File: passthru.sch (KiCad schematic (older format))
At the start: 0 parts

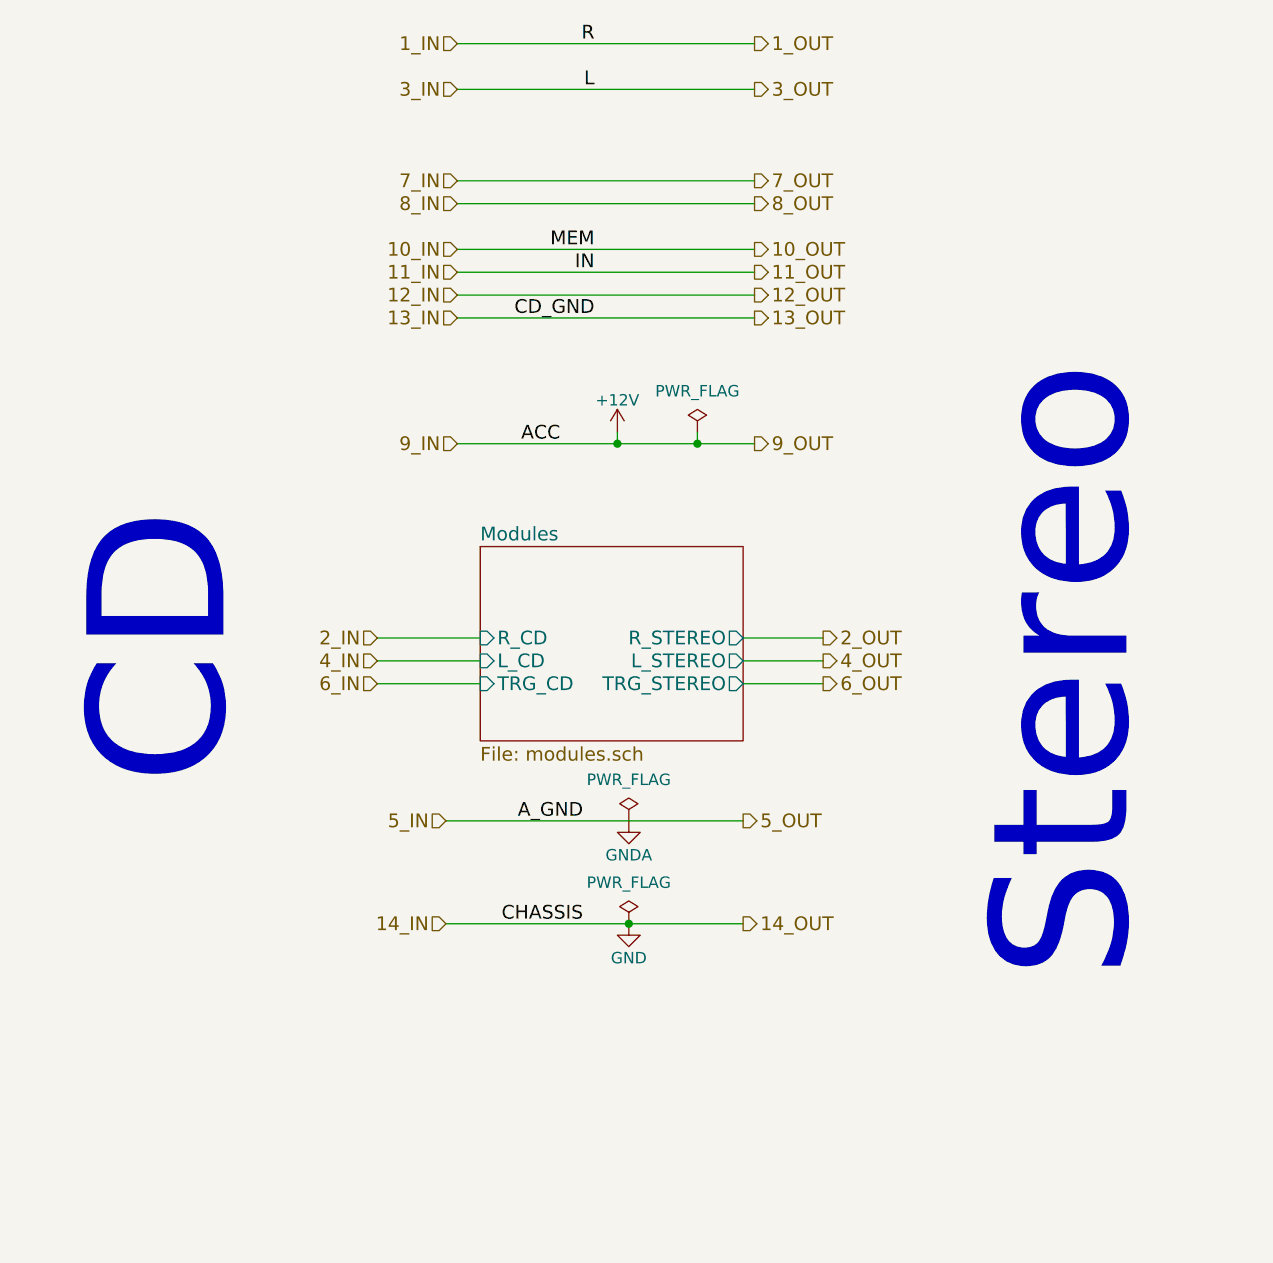
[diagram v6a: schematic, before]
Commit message: Major update to use Atmel ATTINY4313
Replace Pro Micro as microcontroller. Mostly contianed within the
control sheet.
Moved LEDs all onto control sheet.
Updated a few capacitors.
Added a reset switch. Still need to decide part.
Updated a few capacitor models for 4.0.7
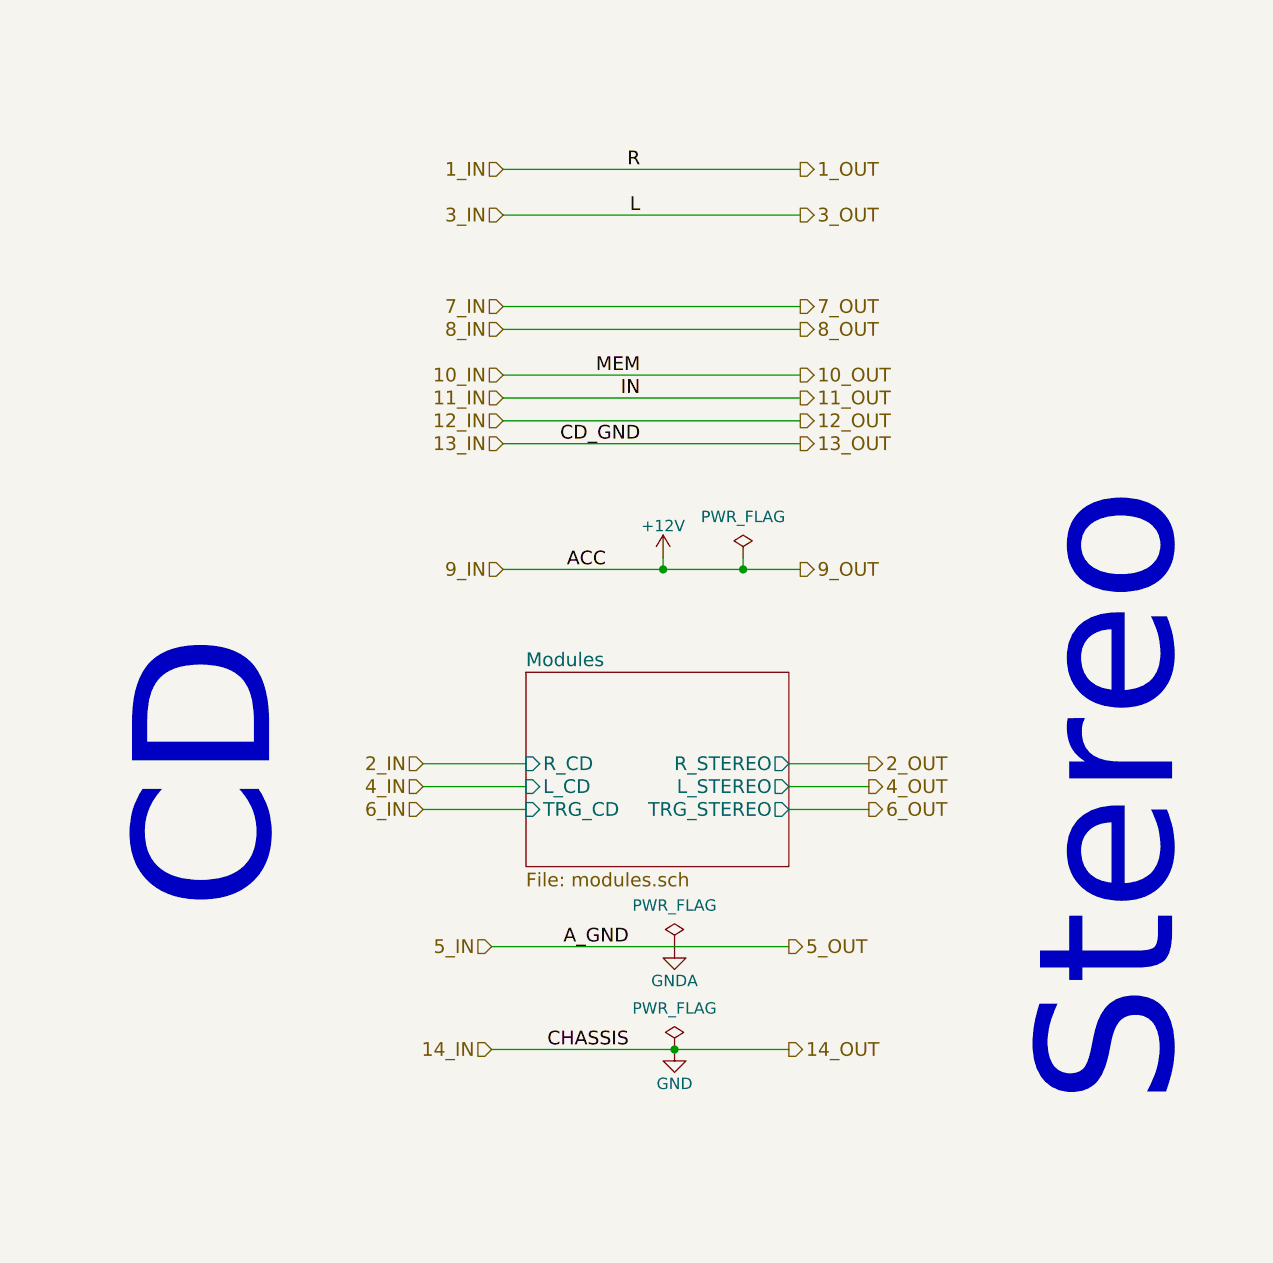
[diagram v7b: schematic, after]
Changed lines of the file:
@@
 $EndDescr
 Wire Wire Line
-	4700 1200 6000 1200
+	4900 1750 6200 1750
 Wire Wire Line
-	4700 1400 6000 1400
+	4900 1950 6200 1950
 Wire Wire Line
-	4650 4600 5950 4600
+	4850 5150 6150 5150
 Wire Wire Line
-	4700 1800 6000 1800
+	4900 2350 6200 2350
 Wire Wire Line
-	4700 1900 6000 1900
+	4900 2450 6200 2450
 Wire Wire Line
-	4700 2950 6000 2950
+	4900 3500 6200 3500
 Wire Wire Line
-	4700 2100 6000 2100
+	4900 2650 6200 2650
 Wire Wire Line
-	4700 2200 6000 2200
+	4900 2750 6200 2750
 Wire Wire Line
-	4700 2300 6000 2300
+	4900 2850 6200 2850
 Wire Wire Line
-	4700 2400 6000 2400
+	4900 2950 6200 2950
 Wire Wire Line
-	4650 5050 5950 5050
-Text HLabel 4700 1200 0    60   Input ~ 0
+	4850 5600 6150 5600
+Text HLabel 4900 1750 0    60   Input ~ 0
 1_IN
-Text HLabel 4350 3800 0    60   Input ~ 0
+Text HLabel 4550 4350 0    60   Input ~ 0
 2_IN
-Text HLabel 4700 1400 0    60   Input ~ 0
+Text HLabel 4900 1950 0    60   Input ~ 0
 3_IN
-Text HLabel 4350 3900 0    60   Input ~ 0
+Text HLabel 4550 4450 0    60   Input ~ 0
 4_IN
-Text HLabel 4650 4600 0    60   Input ~ 0
+Text HLabel 4850 5150 0    60   Input ~ 0
 5_IN
-Text HLabel 4350 4000 0    60   Input ~ 0
+Text HLabel 4550 4550 0    60   Input ~ 0
 6_IN
-Text HLabel 4700 1800 0    60   Input ~ 0
+Text HLabel 4900 2350 0    60   Input ~ 0
 7_IN
-Text HLabel 4700 1900 0    60   Input ~ 0
+Text HLabel 4900 2450 0    60   Input ~ 0
 8_IN
-Text HLabel 4700 2950 0    60   Input ~ 0
+Text HLabel 4900 3500 0    60   Input ~ 0
 9_IN
-Text HLabel 4700 2100 0    60   Input ~ 0
+Text HLabel 4900 2650 0    60   Input ~ 0
 10_IN
-Text HLabel 4700 2200 0    60   Input ~ 0
+Text HLabel 4900 2750 0    60   Input ~ 0
 11_IN
-Text HLabel 4700 2300 0    60   Input ~ 0
+Text HLabel 4900 2850 0    60   Input ~ 0
 12_IN
-Text HLabel 4700 2400 0    60   Input ~ 0
+Text HLabel 4900 2950 0    60   Input ~ 0
 13_IN
-Text HLabel 4650 5050 0    60   Input ~ 0
+Text HLabel 4850 5600 0    60   Input ~ 0
 14_IN
-Text HLabel 6000 1200 2    60   Output ~ 0
+Text HLabel 6200 1750 2    60   Output ~ 0
 1_OUT
-Text HLabel 6300 3800 2    60   Output ~ 0
+Text HLabel 6500 4350 2    60   Output ~ 0
 2_OUT
-Text HLabel 6000 1400 2    60   Output ~ 0
+Text HLabel 6200 1950 2    60   Output ~ 0
 3_OUT
-Text HLabel 6300 3900 2    60   Output ~ 0
+Text HLabel 6500 4450 2    60   Output ~ 0
 4_OUT
-Text HLabel 5950 4600 2    60   Output ~ 0
+Text HLabel 6150 5150 2    60   Output ~ 0
 5_OUT
-Text HLabel 6300 4000 2    60   Output ~ 0
+Text HLabel 6500 4550 2    60   Output ~ 0
 6_OUT
-Text HLabel 6000 1800 2    60   Output ~ 0
+Text HLabel 6200 2350 2    60   Output ~ 0
 7_OUT
-Text HLabel 6000 1900 2    60   Output ~ 0
+Text HLabel 6200 2450 2    60   Output ~ 0
 8_OUT
-Text HLabel 6000 2950 2    60   Output ~ 0
+Text HLabel 6200 3500 2    60   Output ~ 0
 9_OUT
-Text HLabel 6000 2100 2    60   Output ~ 0
+Text HLabel 6200 2650 2    60   Output ~ 0
 10_OUT
-Text HLabel 6000 2200 2    60   Output ~ 0
+Text HLabel 6200 2750 2    60   Output ~ 0
 11_OUT
-Text HLabel 6000 2300 2    60   Output ~ 0
+Text HLabel 6200 2850 2    60   Output ~ 0
 12_OUT
-Text HLabel 6000 2400 2    60   Output ~ 0
+Text HLabel 6200 2950 2    60   Output ~ 0
 13_OUT
-Text HLabel 5950 5050 2    60   Output ~ 0
+Text HLabel 6150 5600 2    60   Output ~ 0
 14_OUT
-Text Label 5300 1200 2    60   ~ 0
+Text Label 5500 1750 2    60   ~ 0
 R
-Text Label 5300 1400 2    60   ~ 0
+Text Label 5500 1950 2    60   ~ 0
 L
-Text Label 5250 4600 2    60   ~ 0
+Text Label 5450 5150 2    60   ~ 0
 A_GND
-Text Label 5150 2950 2    60   ~ 0
+Text Label 5350 3500 2    60   ~ 0
 ACC
-Text Label 5300 2100 2    60   ~ 0
+Text Label 5500 2650 2    60   ~ 0
 MEM
-Text Label 5300 2200 2    60   ~ 0
+Text Label 5500 2750 2    60   ~ 0
 IN
-Text Label 5300 2400 2    60   ~ 0
+Text Label 5500 2950 2    60   ~ 0
 CD_GND
-Text Label 5250 5050 2    60   ~ 0
+Text Label 5450 5600 2    60   ~ 0
 CHASSIS
 Wire Wire Line
-	4350 3800 4800 3800
+	4550 4350 5000 4350
 Wire Wire Line
-	4350 3900 4800 3900
+	4550 4450 5000 4450
 Wire Wire Line
-	4350 4000 4800 4000
+	4550 4550 5000 4550
 Wire Wire Line
-	5950 3800 6300 3800
+	6150 4350 6500 4350
 Wire Wire Line
-	5950 3900 6300 3900
+	6150 4450 6500 4450
 Wire Wire Line
-	5950 4000 6300 4000
+	6150 4550 6500 4550
 $Sheet
-S 4800 3400 1150 850
+S 5000 3950 1150 850
 U 58B1273D
 F0 "Modules" 60
 F1 "modules.sch" 60
-F2 "L_CD" I L 4800 3900 60
-F3 "R_CD" I L 4800 3800 60
-F4 "L_STEREO" O R 5950 3900 60
-F5 "R_STEREO" O R 5950 3800 60
-F6 "TRG_STEREO" O R 5950 4000 60
-F7 "TRG_CD" I L 4800 4000 60
+F2 "L_CD" I L 5000 4450 60
+F3 "R_CD" I L 5000 4350 60
+F4 "L_STEREO" O R 6150 4450 60
+F5 "R_STEREO" O R 6150 4350 60
+F6 "TRG_STEREO" O R 6150 4550 60
+F7 "TRG_CD" I L 5000 4550 60
 $EndSheet
 $Comp
 L GND #PWR01
 U 1 1 58B1285E
-P 5450 5050
-F 0 "#PWR01" H 5450 4800 50  0001 C CNN
-F 1 "GND" H 5450 4900 50  0000 C CNN
-F 2 "" H 5450 5050 50  0000 C CNN
-F 3 "" H 5450 5050 50  0000 C CNN
-	1    5450 5050
+P 5650 5600
+F 0 "#PWR01" H 5650 5350 50  0001 C CNN
+F 1 "GND" H 5650 5450 50  0000 C CNN
+F 2 "" H 5650 5600 50  0000 C CNN
+F 3 "" H 5650 5600 50  0000 C CNN
+	1    5650 5600
 	1    0    0    -1
 $EndComp
-Connection ~ 5450 5050
+Connection ~ 5650 5600
 $Comp
 L PWR_FLAG #FLG02
 U 1 1 58B12AA7
-P 5750 2900
-F 0 "#FLG02" H 5750 2995 50  0001 C CNN
-F 1 "PWR_FLAG" H 5750 3080 50  0000 C CNN
-F 2 "" H 5750 2900 50  0000 C CNN
-F 3 "" H 5750 2900 50  0000 C CNN
-	1    5750 2900
+P 5950 3450
+F 0 "#FLG02" H 5950 3545 50  0001 C CNN
+F 1 "PWR_FLAG" H 5950 3630 50  0000 C CNN
+F 2 "" H 5950 3450 50  0000 C CNN
+F 3 "" H 5950 3450 50  0000 C CNN
+	1    5950 3450
 	1    0    0    -1
 $EndComp
@@
 L +12V #PWR03
 U 1 1 58B12C1E
-P 5400 2900
-F 0 "#PWR03" H 5400 2750 50  0001 C CNN
-F 1 "+12V" H 5400 3040 50  0000 C CNN
-F 2 "" H 5400 2900 50  0000 C CNN
-F 3 "" H 5400 2900 50  0000 C CNN
-	1    5400 2900
+P 5600 3450
+F 0 "#PWR03" H 5600 3300 50  0001 C CNN
+F 1 "+12V" H 5600 3590 50  0000 C CNN
+F 2 "" H 5600 3450 50  0000 C CNN
+F 3 "" H 5600 3450 50  0000 C CNN
+	1    5600 3450
 	1    0    0    -1
 $EndComp
 Wire Wire Line
-	5750 2900 5750 2950
-Connection ~ 5750 2950
+	5950 3450 5950 3500
+Connection ~ 5950 3500
 Wire Wire Line
-	5400 2900 5400 2950
-Connection ~ 5400 2950
+	5600 3450 5600 3500
+Connection ~ 5600 3500
 $Comp
 L PWR_FLAG #FLG04
 U 1 1 58B12B41
-P 5450 5050
-F 0 "#FLG04" H 5450 5145 50  0001 C CNN
-F 1 "PWR_FLAG" H 5450 5230 50  0000 C CNN
-F 2 "" H 5450 5050 50  0000 C CNN
-F 3 "" H 5450 5050 50  0000 C CNN
-	1    5450 5050
+P 5650 5600
+F 0 "#FLG04" H 5650 5695 50  0001 C CNN
+F 1 "PWR_FLAG" H 5650 5780 50  0000 C CNN
+F 2 "" H 5650 5600 50  0000 C CNN
+F 3 "" H 5650 5600 50  0000 C CNN
+	1    5650 5600
 	1    0    0    -1
 $EndComp
-Text Notes 3750 4450 1    600  ~ 0
+Text Notes 3950 5000 1    600  ~ 0
 CD
-Text Notes 7700 5300 1    600  ~ 0
+Text Notes 7900 5850 1    600  ~ 0
 Stereo
 $Comp
 L GNDA #PWR05
 U 1 1 59C094BB
-P 5450 4600
-F 0 "#PWR05" H 5450 4350 50  0001 C CNN
-F 1 "GNDA" H 5450 4450 50  0000 C CNN
-F 2 "" H 5450 4600 50  0000 C CNN
-F 3 "" H 5450 4600 50  0000 C CNN
-	1    5450 4600
+P 5650 5150
+F 0 "#PWR05" H 5650 4900 50  0001 C CNN
+F 1 "GNDA" H 5650 5000 50  0000 C CNN
+F 2 "" H 5650 5150 50  0000 C CNN
+F 3 "" H 5650 5150 50  0000 C CNN
+	1    5650 5150
 	1    0    0    -1
 $EndComp
@@
 L PWR_FLAG #FLG06
 U 1 1 59C09583
-P 5450 4600
-F 0 "#FLG06" H 5450 4695 50  0001 C CNN
-F 1 "PWR_FLAG" H 5450 4780 50  0000 C CNN
-F 2 "" H 5450 4600 50  0000 C CNN
-F 3 "" H 5450 4600 50  0000 C CNN
-	1    5450 4600
+P 5650 5150
+F 0 "#FLG06" H 5650 5245 50  0001 C CNN
+F 1 "PWR_FLAG" H 5650 5330 50  0000 C CNN
+F 2 "" H 5650 5150 50  0000 C CNN
+F 3 "" H 5650 5150 50  0000 C CNN
+	1    5650 5150
 	1    0    0    -1
 $EndComp

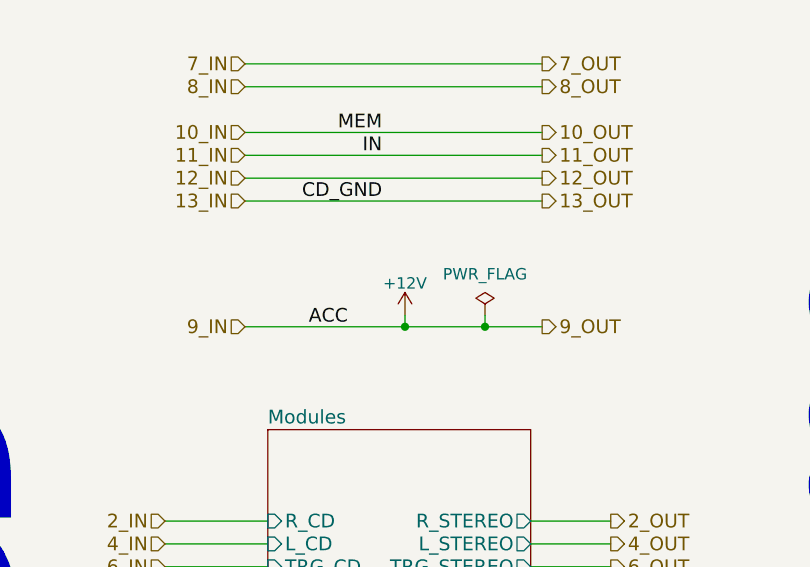
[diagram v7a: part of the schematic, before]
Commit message: Clean up some schematics for readability.
Run 12V from after power protection diode.
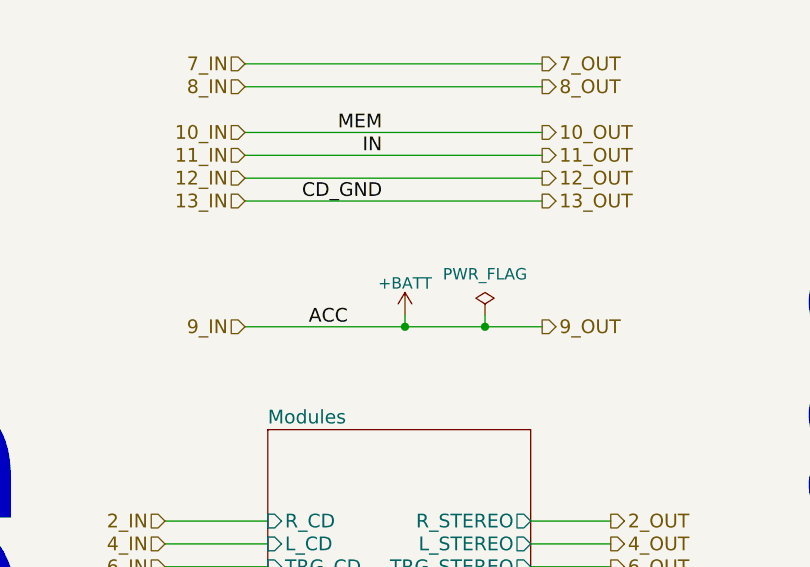
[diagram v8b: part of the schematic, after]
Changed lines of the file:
@@
-	1    0    0    -1
-$EndComp
-$Comp
-L +12V #PWR03
-U 1 1 58B12C1E
-P 5600 3450
-F 0 "#PWR03" H 5600 3300 50  0001 C CNN
-F 1 "+12V" H 5600 3590 50  0000 C CNN
-F 2 "" H 5600 3450 50  0000 C CNN
-F 3 "" H 5600 3450 50  0000 C CNN
-	1    5600 3450
 	1    0    0    -1
 $EndComp
@@
 	1    0    0    -1
 $EndComp
+$Comp
+L +BATT #PWR?
+U 1 1 5A376DB3
+P 5600 3450
+F 0 "#PWR?" H 5600 3300 50  0001 C CNN
+F 1 "+BATT" H 5600 3590 50  0000 C CNN
+F 2 "" H 5600 3450 50  0001 C CNN
+F 3 "" H 5600 3450 50  0001 C CNN
+	1    5600 3450
+	1    0    0    -1
+$EndComp
